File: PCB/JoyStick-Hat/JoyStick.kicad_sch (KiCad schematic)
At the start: 8 parts, among them J10 Conn_01x02_Pin, J11 Conn_01x02_Pin, J4 Conn_01x03_Pin, J5 Conn_01x03_Pin, J6 Conn_01x04_Pin, J7 Conn_01x02_Pin, J8 Conn_01x02_Pin, J9 Conn_01x04_Pin

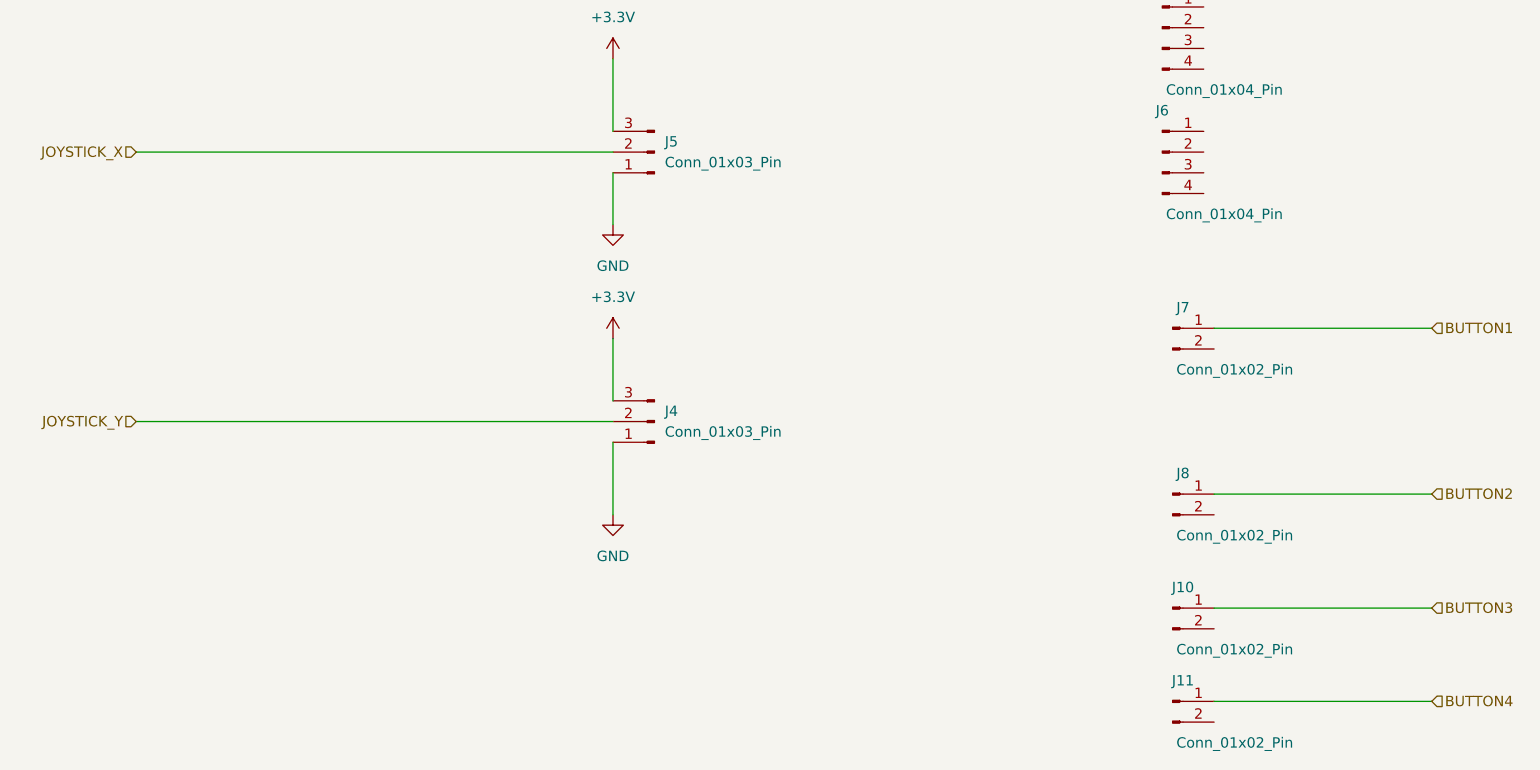
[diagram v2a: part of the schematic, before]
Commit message: Schematic Progress
Made progress with schematic and corrected designator letters with connectors to match the built in paradigm of using J instead of T. T will not be used to referencing transformers instead of connectors.
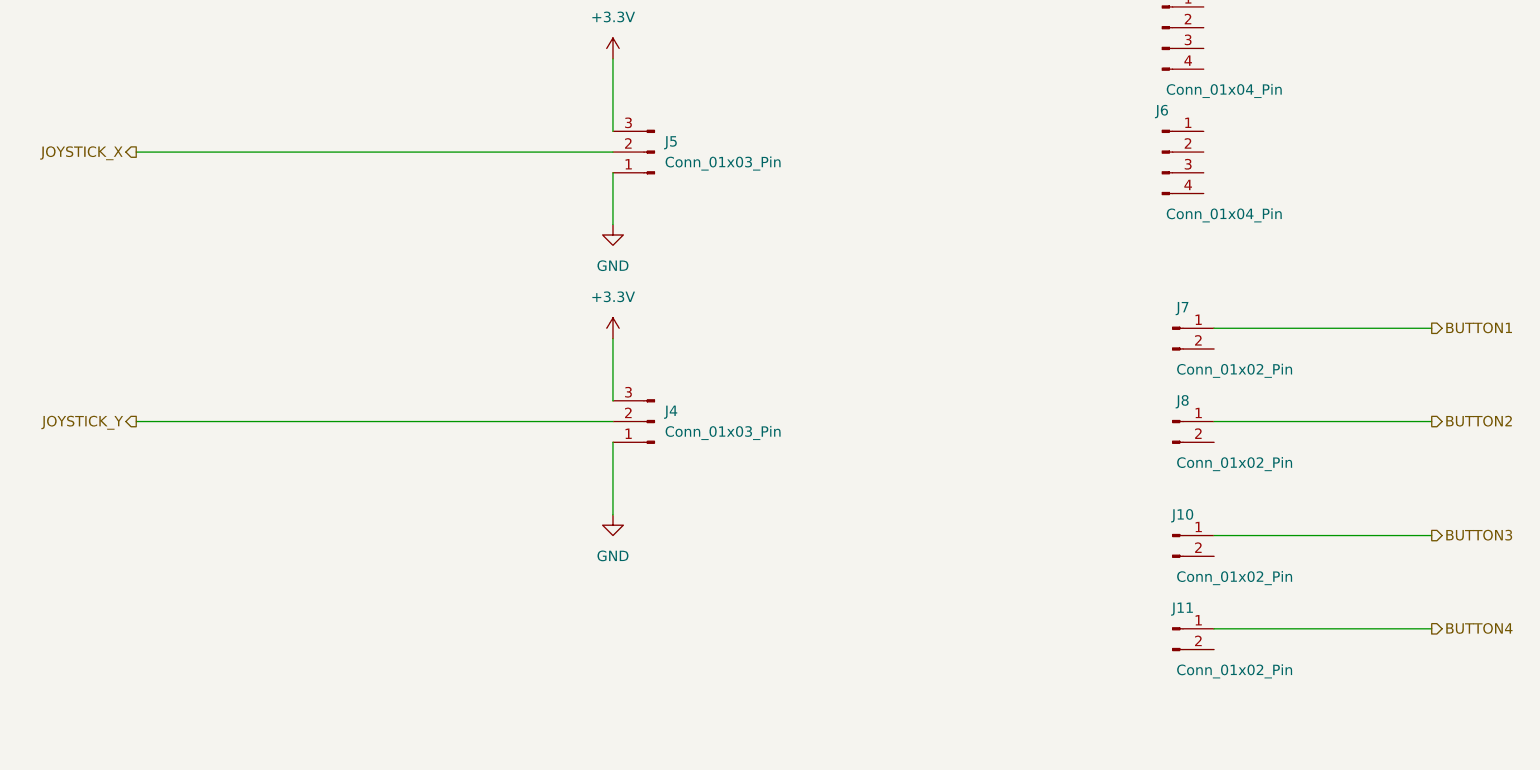
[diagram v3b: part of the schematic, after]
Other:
- moved on the sheet: J10, J11, J8
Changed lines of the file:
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@@
 (kicad_sch (version 20230121) (generator eeschema)
   (paper "A4")
-  (wire (pts (xy 176.53 121.92) (xy 203.2 121.92))
+  (wire (pts (xy 176.53 113.03) (xy 203.2 113.03))
     (stroke (width 0) (type default))
   )
@@
     (stroke (width 0) (type default))
   )
-  (wire (pts (xy 176.53 147.32) (xy 203.2 147.32))
+  (wire (pts (xy 176.53 138.43) (xy 203.2 138.43))
     (stroke (width 0) (type default))
   )
@@
     (stroke (width 0) (type default))
   )
-  (wire (pts (xy 176.53 135.89) (xy 203.2 135.89))
-    (stroke (width 0) (type default))
-  )
-  (hierarchical_label "BUTTON3" (shape input) (at 203.2 135.89 0) (fields_autoplaced)
+  (wire (pts (xy 176.53 127) (xy 203.2 127))
+    (stroke (width 0) (type default))
+  )
+  (hierarchical_label "BUTTON3" (shape output) (at 203.2 127 0) (fields_autoplaced)
     (effects (font (size 1.27 1.27)) (justify left))
   )
-  (hierarchical_label "BUTTON2" (shape input) (at 203.2 121.92 0) (fields_autoplaced)
+  (hierarchical_label "BUTTON2" (shape output) (at 203.2 113.03 0) (fields_autoplaced)
     (effects (font (size 1.27 1.27)) (justify left))
   )
-  (hierarchical_label "JOYSTICK_X" (shape input) (at 44.45 80.01 180) (fields_autoplaced)
+  (hierarchical_label "JOYSTICK_X" (shape output) (at 44.45 80.01 180) (fields_autoplaced)
     (effects (font (size 1.27 1.27)) (justify right))
   )
-  (hierarchical_label "JOYSTICK_Y" (shape input) (at 44.45 113.03 180) (fields_autoplaced)
+  (hierarchical_label "JOYSTICK_Y" (shape output) (at 44.45 113.03 180) (fields_autoplaced)
     (effects (font (size 1.27 1.27)) (justify right))
   )
-  (hierarchical_label "BUTTON1" (shape input) (at 203.2 101.6 0) (fields_autoplaced)
+  (hierarchical_label "BUTTON1" (shape output) (at 203.2 101.6 0) (fields_autoplaced)
     (effects (font (size 1.27 1.27)) (justify left))
   )
-  (hierarchical_label "BUTTON4" (shape input) (at 203.2 147.32 0) (fields_autoplaced)
+  (hierarchical_label "BUTTON4" (shape output) (at 203.2 138.43 0) (fields_autoplaced)
     (effects (font (size 1.27 1.27)) (justify left))
   )
@@
     )
   )
-  (symbol (lib_id "Connector:Conn_01x02_Pin") (at 171.45 121.92 0) (unit 1)
-    (in_bom yes) (on_board yes) (dnp no)
-    (property "Reference" "J8" (at 172.72 119.38 0)
-      (effects (font (size 1.27 1.27)))
-    )
-    (property "Value" "Conn_01x02_Pin" (at 179.07 127 0)
-      (effects (font (size 1.27 1.27)))
-    )
-    (property "Footprint" "" (at 171.45 121.92 0)
-      (effects (font (size 1.27 1.27)) hide)
-    )
-    (property "Datasheet" "~" (at 171.45 121.92 0)
+  (symbol (lib_id "Connector:Conn_01x02_Pin") (at 171.45 113.03 0) (unit 1)
+    (in_bom yes) (on_board yes) (dnp no)
+    (property "Reference" "J8" (at 172.72 110.49 0)
+      (effects (font (size 1.27 1.27)))
+    )
+    (property "Value" "Conn_01x02_Pin" (at 179.07 118.11 0)
+      (effects (font (size 1.27 1.27)))
+    )
+    (property "Footprint" "" (at 171.45 113.03 0)
+      (effects (font (size 1.27 1.27)) hide)
+    )
+    (property "Datasheet" "~" (at 171.45 113.03 0)
       (effects (font (size 1.27 1.27)) hide)
     )
@@
     )
   )
-  (symbol (lib_id "Connector:Conn_01x02_Pin") (at 171.45 135.89 0) (unit 1)
-    (in_bom yes) (on_board yes) (dnp no)
-    (property "Reference" "J10" (at 172.72 133.35 0)
-      (effects (font (size 1.27 1.27)))
-    )
-    (property "Value" "Conn_01x02_Pin" (at 179.07 140.97 0)
-      (effects (font (size 1.27 1.27)))
-    )
-    (property "Footprint" "" (at 171.45 135.89 0)
-      (effects (font (size 1.27 1.27)) hide)
-    )
-    (property "Datasheet" "~" (at 171.45 135.89 0)
+  (symbol (lib_id "Connector:Conn_01x02_Pin") (at 171.45 127 0) (unit 1)
+    (in_bom yes) (on_board yes) (dnp no)
+    (property "Reference" "J10" (at 172.72 124.46 0)
+      (effects (font (size 1.27 1.27)))
+    )
+    (property "Value" "Conn_01x02_Pin" (at 179.07 132.08 0)
+      (effects (font (size 1.27 1.27)))
+    )
+    (property "Footprint" "" (at 171.45 127 0)
+      (effects (font (size 1.27 1.27)) hide)
+    )
+    (property "Datasheet" "~" (at 171.45 127 0)
       (effects (font (size 1.27 1.27)) hide)
     )
@@
     )
   )
-  (symbol (lib_id "Connector:Conn_01x02_Pin") (at 171.45 147.32 0) (unit 1)
-    (in_bom yes) (on_board yes) (dnp no)
-    (property "Reference" "J11" (at 172.72 144.78 0)
-      (effects (font (size 1.27 1.27)))
-    )
-    (property "Value" "Conn_01x02_Pin" (at 179.07 152.4 0)
-      (effects (font (size 1.27 1.27)))
-    )
-    (property "Footprint" "" (at 171.45 147.32 0)
-      (effects (font (size 1.27 1.27)) hide)
-    )
-    (property "Datasheet" "~" (at 171.45 147.32 0)
-      (effects (font (size 1.27 1.27)) hide)
-    )
+  (symbol (lib_id "Connector:Conn_01x02_Pin") (at 171.45 138.43 0) (unit 1)
+    (in_bom yes) (on_board yes) (dnp no)
+    (property "Reference" "J11" (at 172.72 135.89 0)
+      (effects (font (size 1.27 1.27)))
+    )
+    (property "Value" "Conn_01x02_Pin" (at 179.07 143.51 0)
+      (effects (font (size 1.27 1.27)))
+    )
+    (property "Footprint" "" (at 171.45 138.43 0)
+      (effects (font (size 1.27 1.27)) hide)
+    )
+    (property "Datasheet" "~" (at 171.45 138.43 0)
+      (effects (font (size 1.27 1.27)) hide)
+    )

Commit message: PCB Created
Schematic and footprint bugs knocked out PCB created and parts imported into board.
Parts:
- J10, J11, J7, J8: footprint (none) -> Connector_PinHeader_2.54mm:PinHeader_1x02_P2.54mm_Vertical
- J4, J5: footprint (none) -> Connector_PinHeader_2.54mm:PinHeader_1x03_P2.54mm_Vertical
- J6, J9: footprint (none) -> Connector_PinHeader_2.54mm:PinHeader_1x04_P2.54mm_Vertical
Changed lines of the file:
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@@
       (effects (font (size 1.27 1.27)))
     )
-    (property "Footprint" "" (at 171.45 101.6 0)
+    (property "Footprint" "Connector_PinHeader_2.54mm:PinHeader_1x02_P2.54mm_Vertical" (at 171.45 101.6 0)
       (effects (font (size 1.27 1.27)) hide)
     )
@@
       (effects (font (size 1.27 1.27)))
     )
-    (property "Footprint" "" (at 171.45 113.03 0)
+    (property "Footprint" "Connector_PinHeader_2.54mm:PinHeader_1x02_P2.54mm_Vertical" (at 171.45 113.03 0)
       (effects (font (size 1.27 1.27)) hide)
     )
@@
       (effects (font (size 1.27 1.27)) (justify right))
     )
-    (property "Footprint" "" (at 107.95 80.01 0)
+    (property "Footprint" "Connector_PinHeader_2.54mm:PinHeader_1x03_P2.54mm_Vertical" (at 107.95 80.01 0)
       (effects (font (size 1.27 1.27)) hide)
     )
@@
       (effects (font (size 1.27 1.27)) (justify right))
     )
-    (property "Footprint" "" (at 107.95 113.03 0)
+    (property "Footprint" "Connector_PinHeader_2.54mm:PinHeader_1x03_P2.54mm_Vertical" (at 107.95 113.03 0)
       (effects (font (size 1.27 1.27)) hide)
     )
@@
       (effects (font (size 1.27 1.27)))
     )
-    (property "Footprint" "" (at 170.18 64.77 0)
+    (property "Footprint" "Connector_PinHeader_2.54mm:PinHeader_1x04_P2.54mm_Vertical" (at 170.18 64.77 0)
       (effects (font (size 1.27 1.27)) hide)
     )
@@
       (effects (font (size 1.27 1.27)))
     )
-    (property "Footprint" "" (at 171.45 127 0)
+    (property "Footprint" "Connector_PinHeader_2.54mm:PinHeader_1x02_P2.54mm_Vertical" (at 171.45 127 0)
       (effects (font (size 1.27 1.27)) hide)
     )
@@
       (effects (font (size 1.27 1.27)))
     )
-    (property "Footprint" "" (at 170.18 80.01 0)
+    (property "Footprint" "Connector_PinHeader_2.54mm:PinHeader_1x04_P2.54mm_Vertical" (at 170.18 80.01 0)
       (effects (font (size 1.27 1.27)) hide)
     )
@@
       (effects (font (size 1.27 1.27)))
     )
-    (property "Footprint" "" (at 171.45 138.43 0)
-      (effects (font (size 1.27 1.27)) hide)
-    )
+    (property "Footprint" "Connector_PinHeader_2.54mm:PinHeader_1x02_P2.54mm_Vertical" (at 171.45 138.43 0)
+      (effects (font (size 1.27 1.27)) hide)
+    )

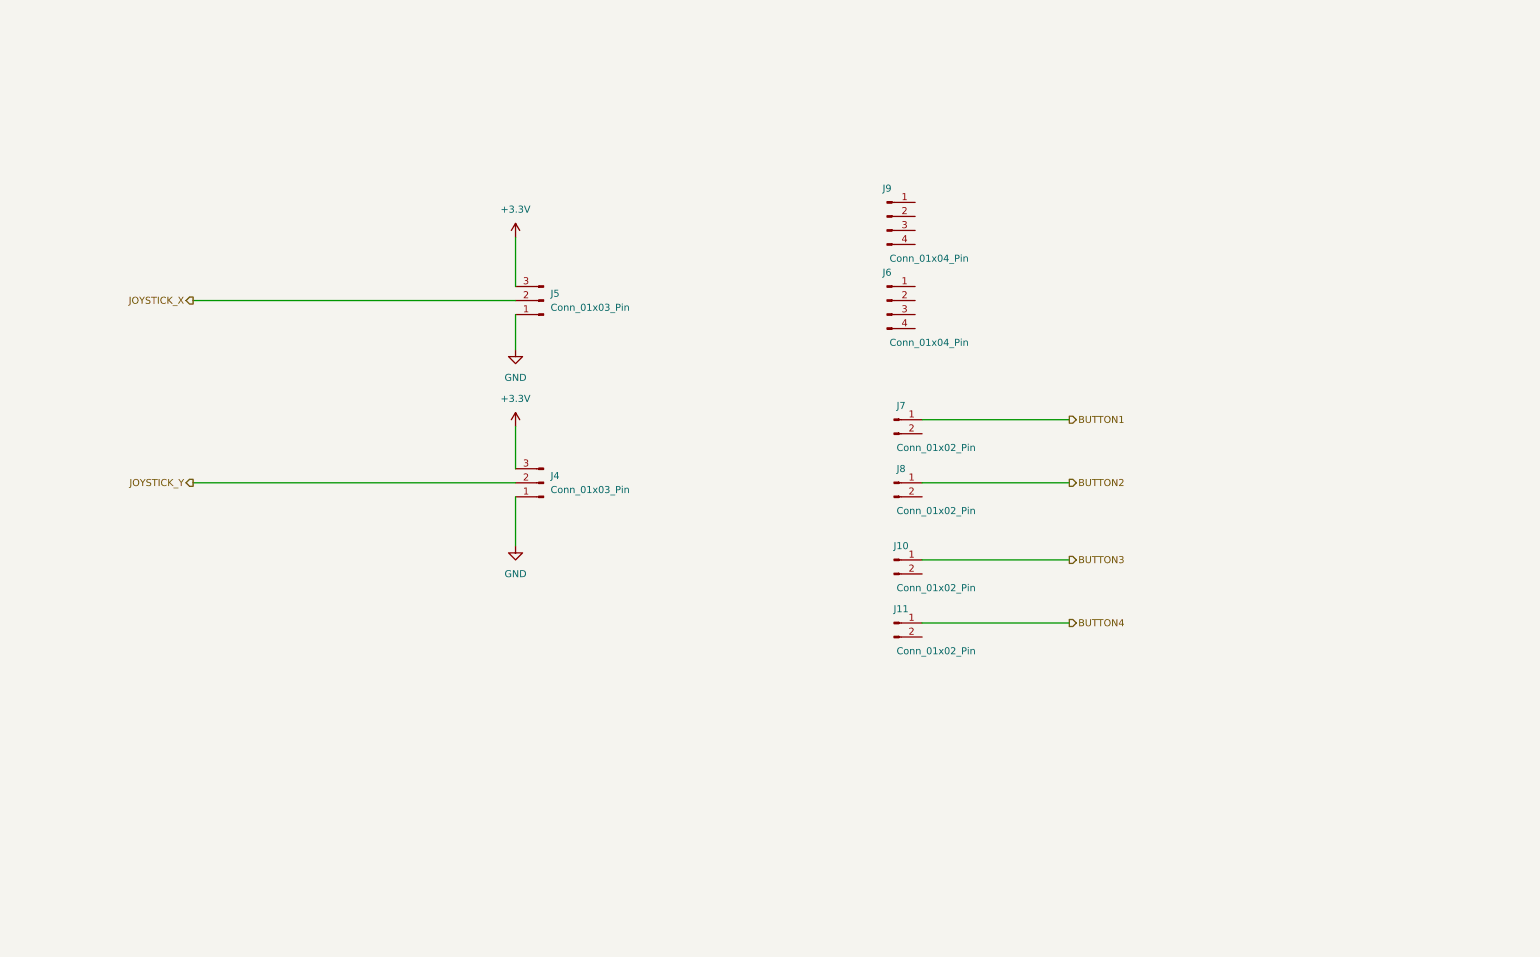
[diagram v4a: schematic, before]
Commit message: LEDs and Additional connectors
Added heartbeat and diagnostic LEDs to STM32 and RPi3 schematics so we can directly flash them for debug purposes. Added a connector for serial port diagnostics on STM32. Added rotary switch interface for STM32 and added pullups to button connectors.
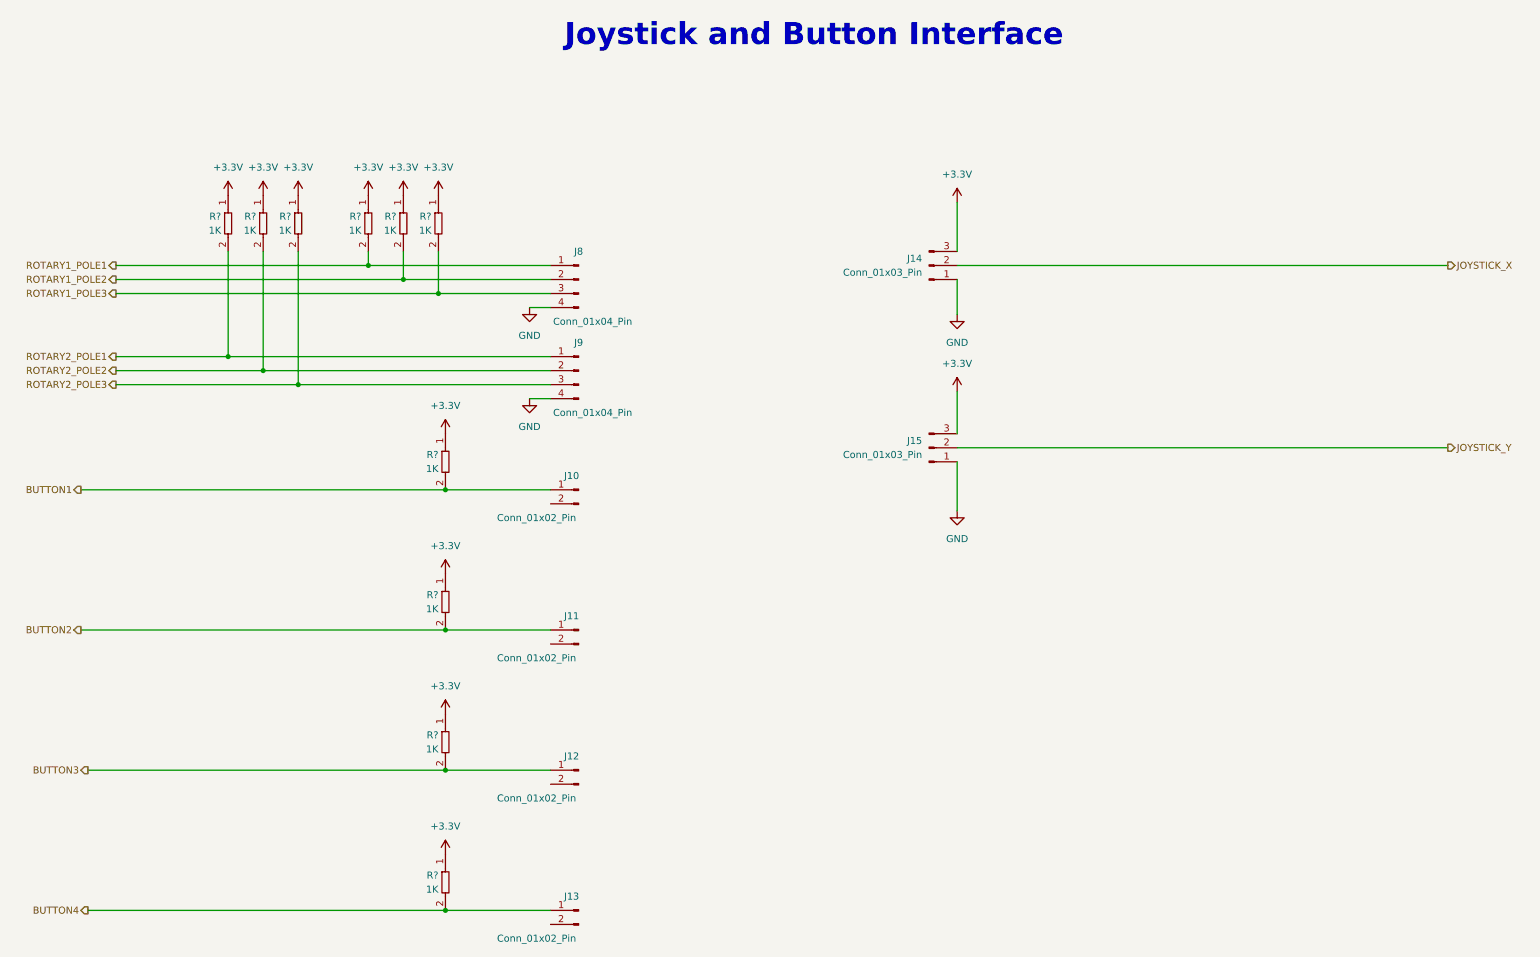
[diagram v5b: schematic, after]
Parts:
- added R? (x10): RC0402FR-071KL, AVR-KiCAD-Lib-Resistors:R0402, symbol AVR-KiCAD-Lib-Resistors:RC0402FR-071KL
- renumbered J7 to J10, J8 to J11, J10 to J12, J11 to J13, J5 to J14, J4 to J15, J9 to J8, J6 to J9
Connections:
- net +3.3V: now also R?.1, R?.1, R?.1, R?.1, R?.1, R?.1, R?.1, R?.1, R?.1, R?.1
- net BUTTON1: now also R?.2
- net BUTTON2: now also R?.2
- net BUTTON3: now also R?.2
- net BUTTON4: now also R?.2
- net GND: now also J8.4 (Pin_4), J9.4 (Pin_4)
- net ROTARY1_POLE1: now reaches J8.1 (Pin_1)
- net ROTARY1_POLE1: now also R?.2
- net ROTARY1_POLE2: now reaches J8.2 (Pin_2)
- net ROTARY1_POLE2: now also R?.2
- net ROTARY1_POLE3: now reaches J8.3 (Pin_3)
- net ROTARY1_POLE3: now also R?.2
- net ROTARY2_POLE1: now reaches J9.1 (Pin_1)
- net ROTARY2_POLE1: now also R?.2
- net ROTARY2_POLE2: now reaches J9.2 (Pin_2)
- net ROTARY2_POLE2: now also R?.2
- net ROTARY2_POLE3: now reaches J9.3 (Pin_3)
- net ROTARY2_POLE3: now also R?.2
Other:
- note added: "Joystick and Button Interface"
- moved on the sheet: J10, J11, J12, J13, J14, J15, J8, J9
